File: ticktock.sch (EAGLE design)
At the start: 64 parts, among them IC1 ATMEGA644A, IC2 AD8611RM, IC3 REF200U, J1 AVR_SPI_PRG_6NS, Q1 MOSFET-NCHANNEL2N7002PW, Q2 MOSFET-NCHANNELBSS138, Q3 MOSFET-NCHANNELBSS138, U1 MAX232SOIC16, U2 OSCILLATORSMD, U3 FT232RLSSOP

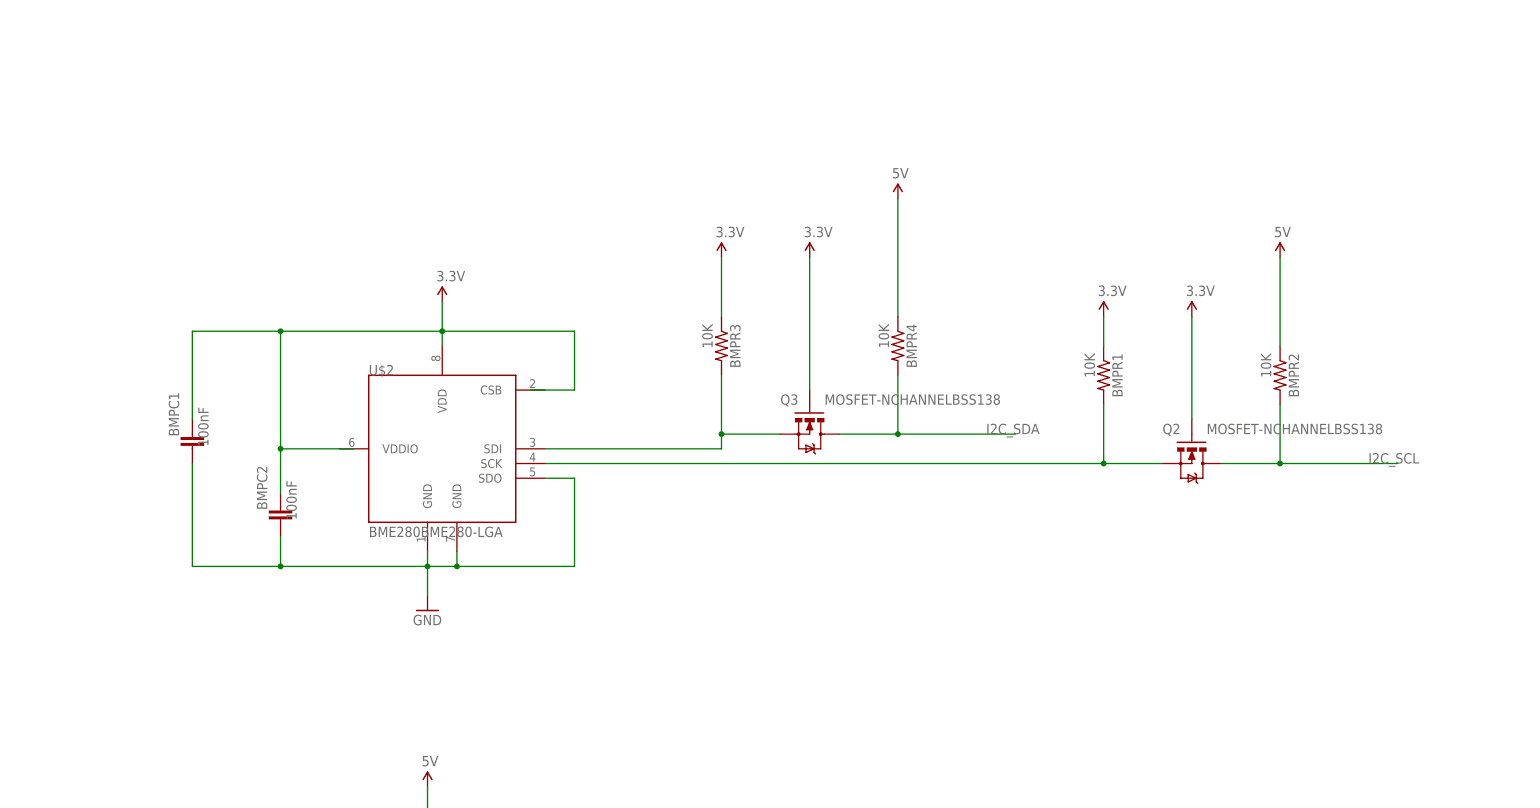
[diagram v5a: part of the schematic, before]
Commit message: Place new BME280 and old BMP180 on board
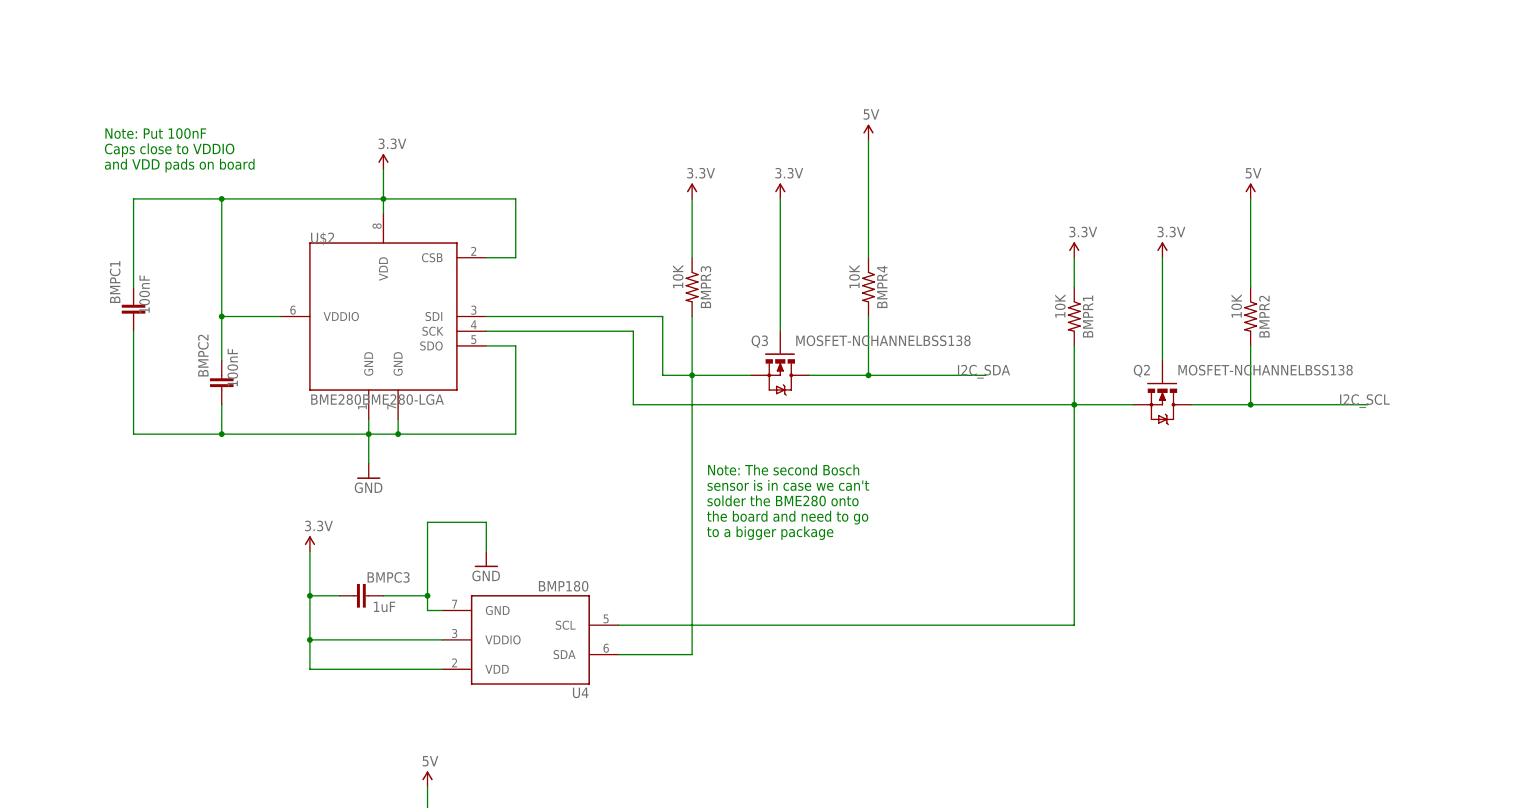
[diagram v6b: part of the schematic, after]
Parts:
- added BMPC3: 1uF, SparkFun-Capacitors:CAP0805
- added U4: BMP180, SparkFun-Sensors:BMP180
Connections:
- removed net N$18: BMPR3.2, Q3.S, U$2.SDI
- new net N$23: BMPR3.2, Q3.S, U$2.SDI, U4.SDA
- net 3.3V: now also BMPC3.1, U$2.CSB, U$2.VDDIO, U4.VDD, U4.VDDIO
- net GND: now also BMPC3.2, U4.GND
- net N$15: now also U4.SCL
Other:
- note added: "Note: Put 100nF Caps close to VDDIO and VDD pads on board"
- note added: "Note: The second Bosch sensor is in case we can't solder the BME280 onto the board and need to go to a bigger package"
- moved on the sheet: BMPC1, BMPC2, BMPR1, BMPR2, BMPR3, BMPR4, Q2, Q3, U$2

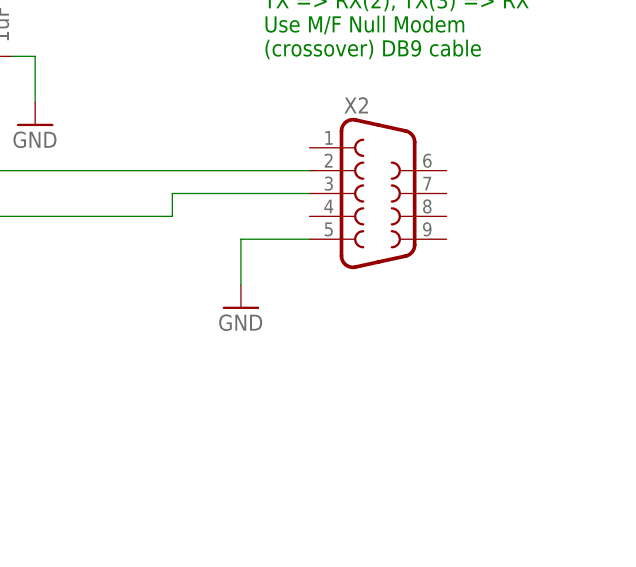
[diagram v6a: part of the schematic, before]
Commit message: Clean up ERC and add pin 1 marker on BME280
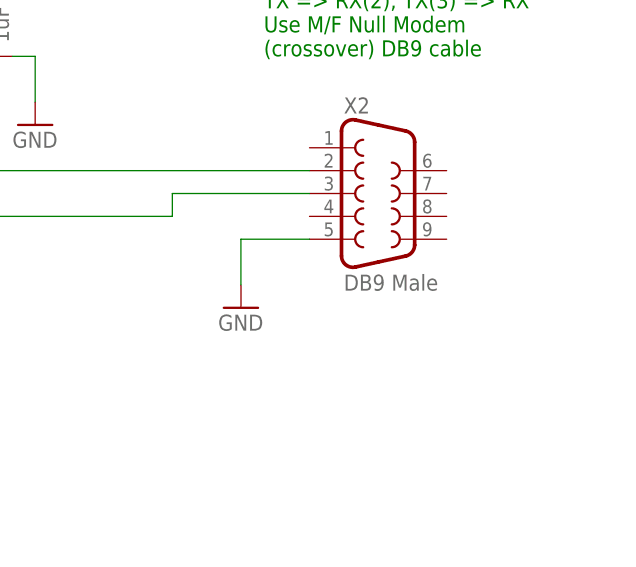
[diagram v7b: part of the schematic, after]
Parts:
- X2: value (none) -> DB9 Male
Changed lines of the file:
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@@
 <part name="STANDOFF4" library="SparkFun-Electromechanical" deviceset="STAND-OFF" device=""/>
 <part name="JP9" library="SparkFun-Connectors" deviceset="M03" device="LOCK" value="3-Pin"/>
-<part name="X2" library="SparkFun-Connectors" deviceset="DB9" device="MALE"/>
+<part name="X2" library="SparkFun-Connectors" deviceset="DB9" device="MALE" value="DB9 Male"/>
 <part name="U$2" library="tickTockLibrary" deviceset="BME280" device="BME280-LGA"/>
 <part name="BMPC2" library="SparkFun-Capacitors" deviceset="CAP" device="0805" value="100nF"/>

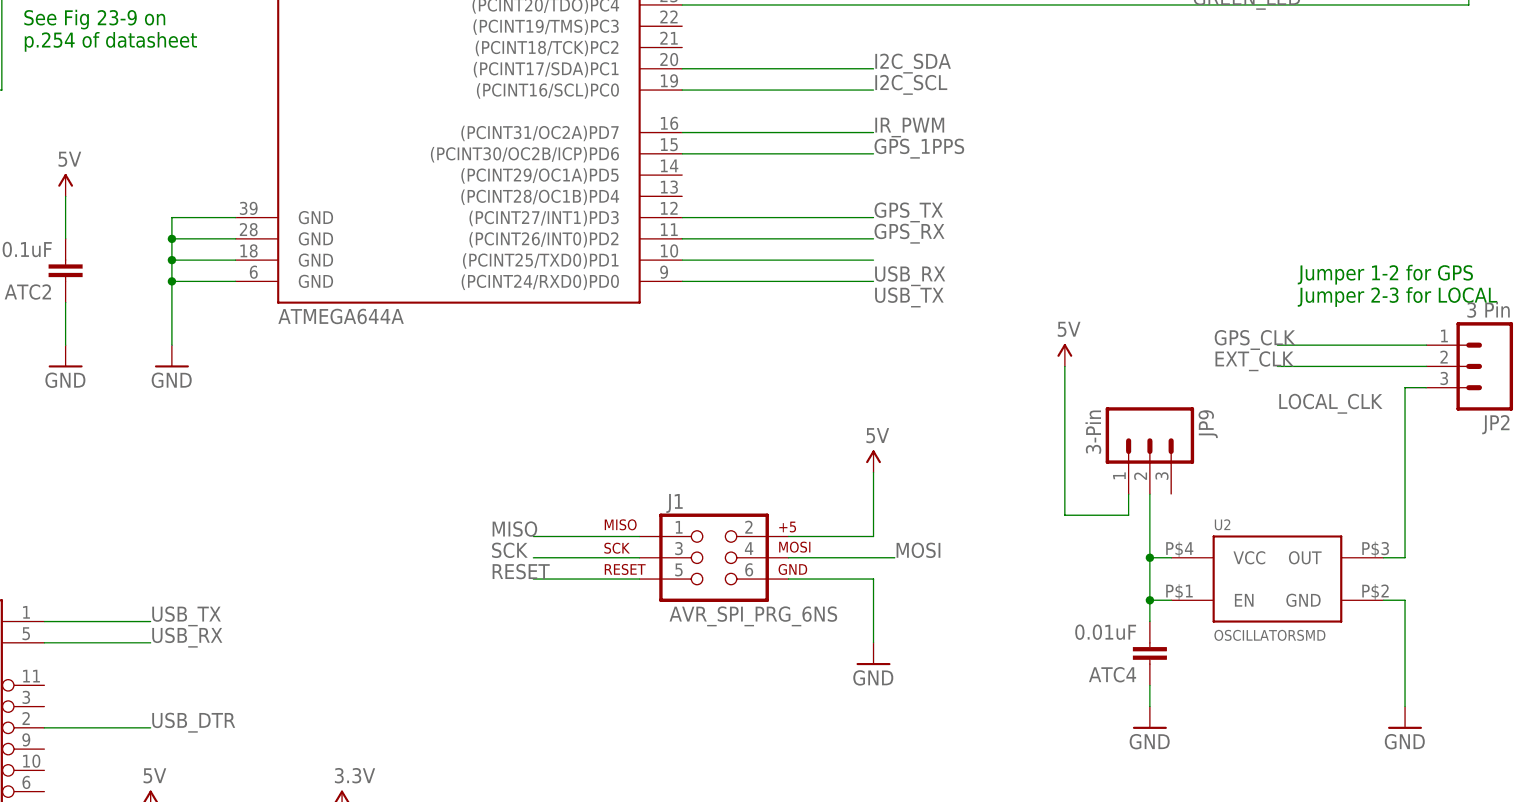
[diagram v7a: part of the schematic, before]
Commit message: Relabel USB_TX and USB_RX to be consistent with MCU's perspective
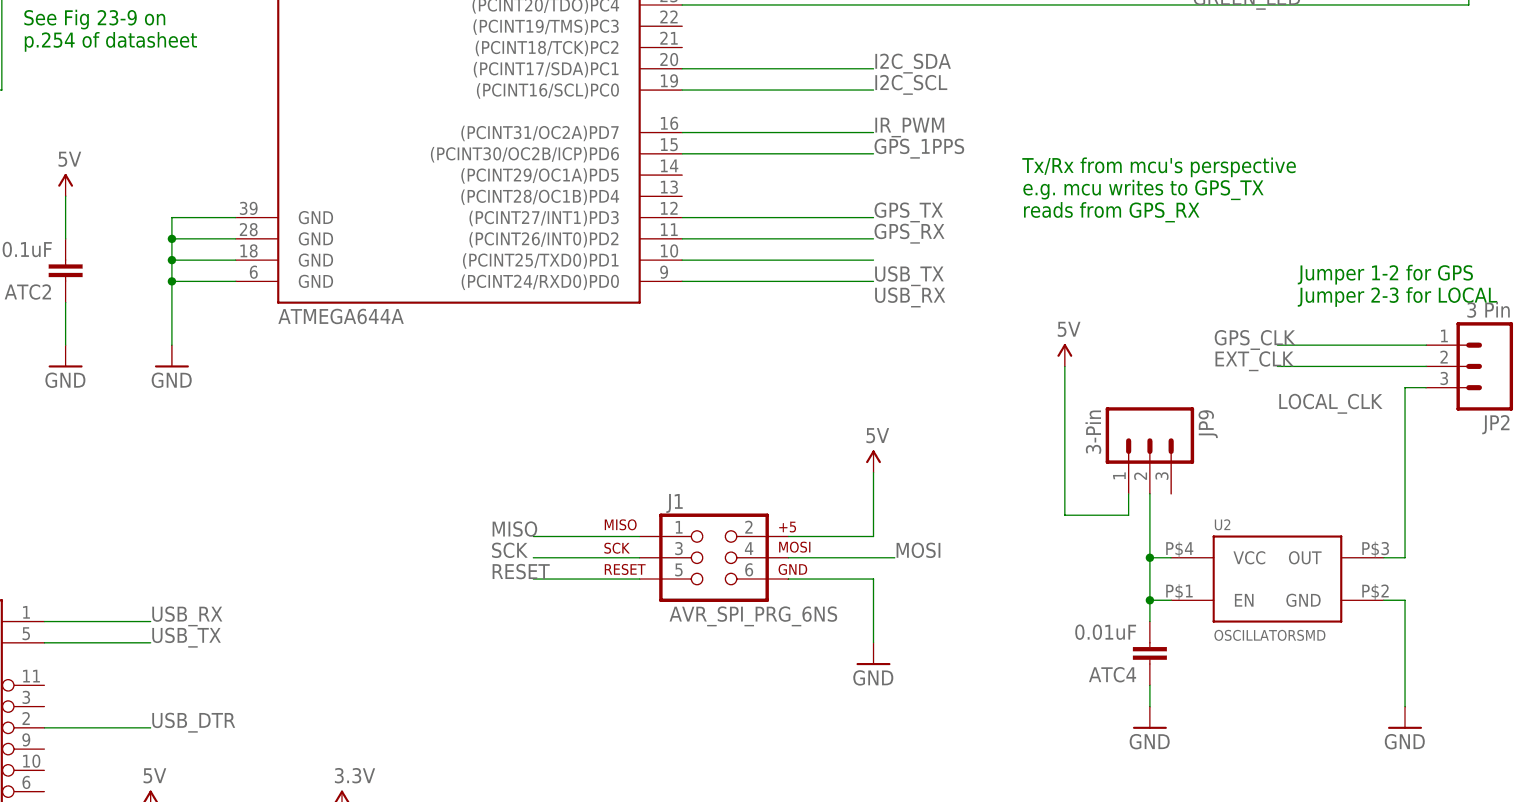
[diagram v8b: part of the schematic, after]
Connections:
- net USB_RX: now also IC1.(PCINT24/RXD0)PD0, U3.TXD; no longer IC1.(PCINT25/TXD0)PD1, U3.RXD
- net USB_TX: now also IC1.(PCINT25/TXD0)PD1, U3.RXD; no longer IC1.(PCINT24/RXD0)PD0, U3.TXD
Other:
- note added: "Tx/Rx from mcu's perspective e.g. mcu writes to GPS_TX reads from GPS_RX"
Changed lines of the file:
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@@
 the board and need to go
 to a bigger package</text>
+<text x="205.74" y="109.22" size="1.778" layer="91">Tx/Rx from mcu's perspective
+e.g. mcu writes to GPS_TX
+reads from GPS_RX</text>
 </plain>
 <instances>
@@
 </segment>
 </net>
-<net name="USB_RX" class="0">
+<net name="USB_TX" class="0">
 <segment>
 <pinref part="IC1" gate="G$1" pin="(PCINT25/TXD0)PD1"/>
@@
 </segment>
 </net>
-<net name="USB_TX" class="0">
+<net name="USB_RX" class="0">
 <segment>
 <pinref part="IC1" gate="G$1" pin="(PCINT24/RXD0)PD0"/>
